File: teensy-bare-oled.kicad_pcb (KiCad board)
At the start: 2 copper layers, 68.7 x 41.2 mm, 6 parts, among them J1 TEENSY-LC, J2 OLED_128x64

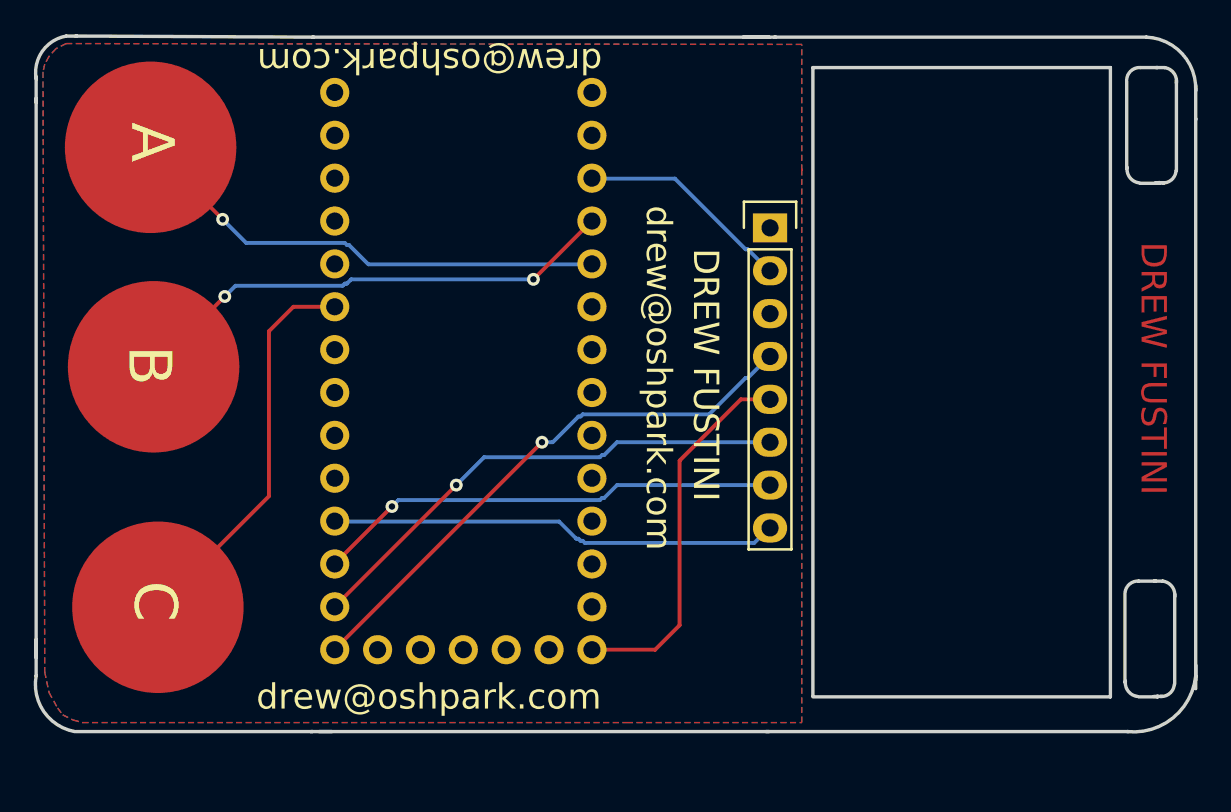
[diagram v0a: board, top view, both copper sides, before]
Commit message: create breakout for er-oled-0.91-1
from:
https://github.com/Agilack/contrib-kicad_parts/tree/master/disp-oled-EastRising

potentially for:
http://www.buydisplay.com/default/0-91-inch-128x32-oled-display-module-serial-spi-ssd1306-white-on-black
http://www.buydisplay.com/default/0-91-inch-128x32-oled-display-with-connector-fpc-ssd1306-white-on-black
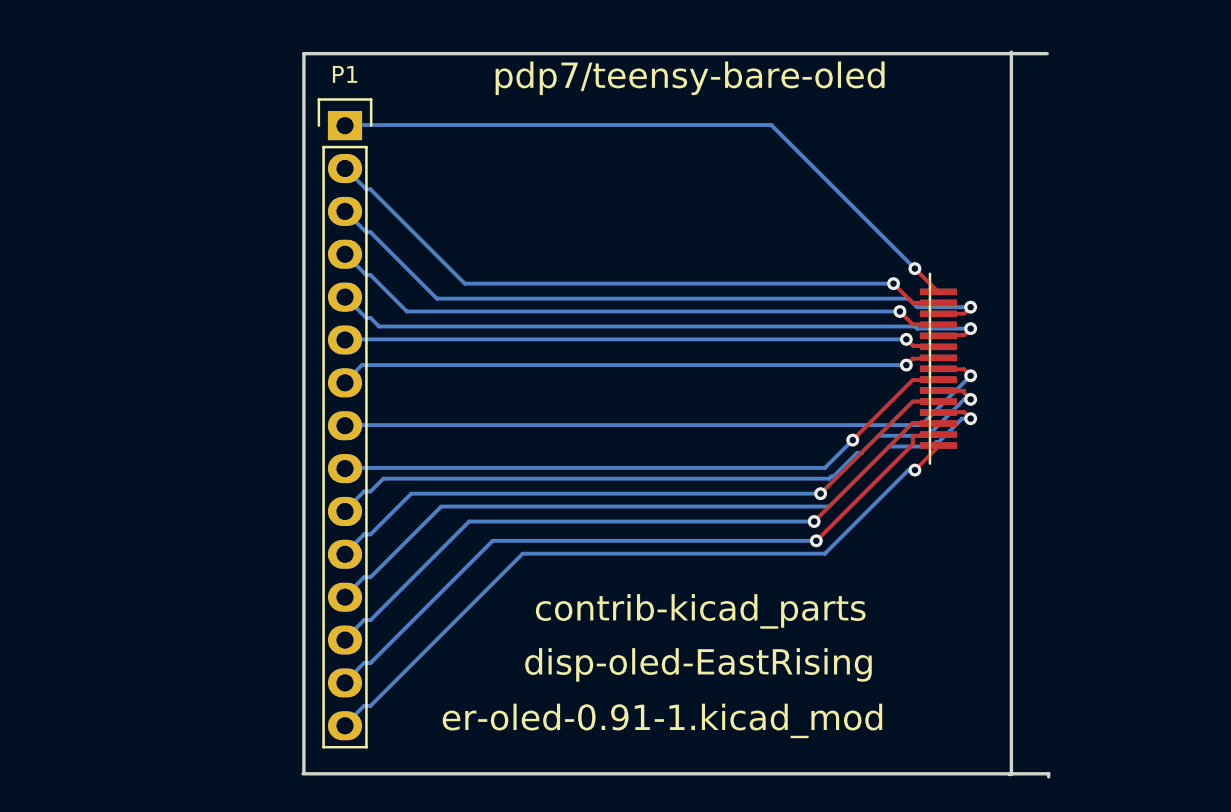
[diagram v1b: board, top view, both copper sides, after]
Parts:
- removed CAP1, CAP2, CAP3: CAPSENSE_CIRCLE, Wickerlib:CAPSENSE_CIRCLE_D10
- removed J1: TEENSY-LC, Wickerlib:TEENSY-LC
- removed J2: OLED_128x64, Wickerlib:Pin_Header_Straight_1x08
- removed REF**: Symbol_OSHW-Logo_SilkScreen, Wickerlib:Symbol_OSHW-Logo_SilkScreen
- added DISP1: ER-OLED0.91-3, disp-oled-EastRising:er-oled-0.91-1, F.Cu at (174.5, 111.2)
- added P1: CONN_01X15, Wickerlib:CONN-HEADER-STRAIGHT-P2.54MM-1x15, F.Cu at (139.0, 96.8)
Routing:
- net Net-(DISP1-Pad12): track 0.00 -> 43.6 mm, vias 0 -> 1
- net Net-(DISP1-Pad15): track 0.00 -> 42.1 mm, vias 0 -> 1
- net Net-(DISP1-Pad10): track 0.00 -> 42.1 mm, vias 0 -> 1
- net Net-(DISP1-Pad14): track 0.00 -> 41.7 mm, vias 0 -> 1
- net Net-(DISP1-Pad3): track 0.00 -> 41.6 mm, vias 0 -> 1
- net Net-(DISP1-Pad13): track 0.00 -> 40.6 mm, vias 0 -> 1
- net Net-(DISP1-Pad8): track 0.00 -> 40.4 mm, vias 0 -> 1
- net Net-(DISP1-Pad5): track 0.00 -> 40.0 mm, vias 0 -> 1
- net Net-(DISP1-Pad1): track 0.00 -> 39.3 mm, vias 0 -> 1
- net Net-(DISP1-Pad11): track 0.00 -> 39.0 mm, vias 0 -> 1
- net Net-(DISP1-Pad2): track 0.00 -> 38.5 mm, vias 0 -> 1
- net Net-(DISP1-Pad9): track 0.00 -> 37.4 mm, vias 0 -> 1
- net Net-(DISP1-Pad4): track 0.00 -> 37.0 mm, vias 0 -> 1
- net Net-(DISP1-Pad7): track 0.00 -> 35.9 mm, vias 0 -> 1
- net Net-(DISP1-Pad6): track 0.00 -> 35.4 mm, vias 0 -> 1
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- removed copper zone on B.Cu, net /GND
- removed copper zone on F.Cu, net /GND
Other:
- board size 68.7 x 41.2 mm -> 44.2 x 42.9 mm
- board text added: "2017-03-01"
- board text added: "contrib-kicad_parts"
- board text added: "disp-oled-EastRising"
- board text added: "er-oled-0.91-1.kicad_mod"
- board text added: "pdp7/teensy-bare-oled"
- board text removed: "A"
- board text removed: "B"
- board text removed: "C"
- board text removed: "DREW FUSTINI"
- board text removed: "drew@oshpark.com"
